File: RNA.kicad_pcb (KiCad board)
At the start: 2 copper layers, 126 x 85 mm, 86 parts, among them J1 USB_B_Micro, J2 AudioJack4, J3 Conn_01x06, SW1 SW_Push, SW11 SW_Push_45deg, SW12 SW_Push_45deg, SW13 SW_Push_45deg, SW14 SW_Push_45deg, SW15 SW_Push_45deg, SW16 SW_Push_45deg, SW2 SW_Push, SW21 SW_Push_45deg, SW22 SW_Push_45deg, SW23 SW_Push_45deg, SW24 SW_Push_45deg, SW25 SW_Push_45deg, SW26 SW_Push_45deg, SW31 SW_Push_45deg, SW32 SW_Push_45deg, SW33 SW_Push_45deg, SW34 SW_Push_45deg, SW35 SW_Push_45deg, SW36 SW_Push_45deg, SW41 SW_Push_45deg, SW42 SW_Push_45deg, SW43 SW_Push_45deg, SW44 SW_Push_45deg, SW45 SW_Push_45deg, SW46 SW_Push_45deg, SW47 SW_Push_45deg, SW51 SW_Push_45deg, SW52 SW_Push_45deg, SW53 SW_Push_45deg, SW54 SW_Push_45deg, SW55 SW_Push_45deg, SW56 SW_Push_45deg, SW57 SW_Push_45deg, U1 STM32F072C8Tx, U2 USBLC6-2SC6, U3 MIC5219-3.3YM5

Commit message: wip"
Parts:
- removed C10, C9: 10u, Capacitor_SMD:C_1206_3216Metric_Pad1.42x1.75mm_HandSolder
- added J4: AudioJack4, Connector_PinHeader_2.54mm:PinHeader_1x04_P2.54mm_Vertical, F.Cu at (133.3, 52.1)
- added R1: R_Small, Resistor_SMD:R_0603_1608Metric, F.Cu at (138.4, 48.0)
- added R2: R_Small, Resistor_SMD:R_0603_1608Metric, F.Cu at (135.9, 48.3)
- added R4: 39k, Resistor_SMD:R_0603_1608Metric, B.Cu at (133.3, 27.9)
- added R7: 68k, Resistor_SMD:R_0603_1608Metric, B.Cu at (133.3, 31.8)
- C1: value 4.7u -> 1u; footprint Capacitor_SMD:C_1206_3216Metric_Pad1.42x1.75mm_HandSolder -> Capacitor_SMD:C_0603_1608Metric
- C2, C3: value 1n -> 100n; footprint Capacitor_SMD:C_0603_1608Metric_Pad1.05x0.95mm_HandSolder -> Capacitor_SMD:C_0603_1608Metric; moved to B.Cu
- C4, J1, U1: moved to B.Cu
- C5: footprint Capacitor_SMD:C_1206_3216Metric_Pad1.42x1.75mm_HandSolder -> Capacitor_SMD:C_0603_1608Metric
- C6, C7: footprint Capacitor_SMD:C_0603_1608Metric_Pad1.05x0.95mm_HandSolder -> Capacitor_SMD:C_0603_1608Metric; moved to B.Cu
- D1: value D_Small -> D_Schottky_Small; footprint Diode_SMD:D_SOD-123 -> Diode_SMD:D_SOD-323
- J2: footprint Connector_Audio:Jack_3.5mm_PJ320E_Horizontal -> Connector_JST:JST_SH_SM04B-SRSS-TB_1x04-1MP_P1.00mm_Horizontal; moved to B.Cu
- J3: footprint Connector_PinSocket_2.54mm:PinSocket_1x06_P2.54mm_Vertical -> Connector_PinHeader_2.54mm:PinHeader_2x03_P2.54mm_Vertical
- R3, R5, R6: footprint Resistor_SMD:R_0603_1608Metric_Pad1.05x0.95mm_HandSolder -> Resistor_SMD:R_0603_1608Metric; moved to B.Cu
- SW1: value SW_Push -> SW_SPST; footprint Button_Switch_SMD:SW_SPST_TL3342 -> Button_Switch_SMD:SW_DIP_SPSTx01_Slide_6.7x4.1mm_W8.61mm_P2.54mm_LowProfile
- SW2: footprint Button_Switch_SMD:SW_SPST_TL3342 -> Button_Switch_SMD:Panasonic_EVQPUL_EVQPUC
- U2: value USBLC6-2SC6 -> PRTR5V0U2X; footprint Package_TO_SOT_SMD:SOT-23-6 -> random-keyboard-parts:SOT143B; moved to B.Cu
- U3: value MIC5219-3.3YM5 -> MCP1703A-3302_SOT23; footprint Package_TO_SOT_SMD:SOT-23-5 -> Package_TO_SOT_SMD:SOT-23
- moved C1 20.6 mm to (131.3, 25.7), turned to 0 degrees
- moved C6 17.2 mm to (130.8, 34.3), turned to 270 degrees
- moved C3 16.9 mm to (138.9, 33.0), turned to 0 degrees
- moved C2 12.9 mm to (143.5, 44.5), turned to 90 degrees
- moved C4 12.6 mm to (132.6, 47.2), turned to 0 degrees
- moved U3 12.4 mm to (133.3, 28.7), turned to 90 degrees
- moved R3 11.5 mm to (141.0, 49.0), turned to 90 degrees
- moved SW2 10.7 mm to (143.5, 67.3)
- moved R5 9.69 mm to (135.9, 61.0)
- moved D1 8.76 mm to (133.3, 32.5), turned to 0 degrees
- moved J3 8.45 mm to (129.5, 63.5)
- moved SW1 8.13 mm to (137.2, 64.8)
- moved J2 7.44 mm to (142.2, 59.7)
- moved R6 7.35 mm to (135.9, 58.4), turned to 180 degrees
- moved U1 6.59 mm to (136.4, 40.2)
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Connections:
- net Net-(U1-Pad39) renamed SWO
- C1 pad 1: VDD -> Net-(C1-Pad1)
- D1 pad 1: Net-(C9-Pad1) -> Net-(C1-Pad1)
- J1 pad 2: Net-(J1-Pad2) -> D-
- J1 pad 3: Net-(J1-Pad3) -> D+
- R5 pad 2: Net-(J2-PadR2) -> Net-(J2-Pad3)
- R6 pad 2: Net-(J2-PadR1) -> Net-(J2-Pad2)
- U1 pad 38: Net-(U1-Pad38) -> VBUS_SENSE
- U1 pad 44: BOOT0 -> Net-(U1-Pad44)
- U1 pad 5: Net-(U1-Pad5) -> BOOT0
- U2 pad 1: Net-(J1-Pad2) -> GND
- U2 pad 2: GND -> D+
- U2 pad 3: Net-(J1-Pad3) -> D-
- U2 pad 4: D+ -> VBUS
- U3 pad 1: Net-(C9-Pad1) -> GND
- U3 pad 2: GND -> VDD
- U3 pad 3: Net-(C9-Pad1) -> Net-(C1-Pad1)
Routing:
- net VBUS_SENSE: track 0.00 -> 2.23 mm
- net (no net): vias 2 -> 0

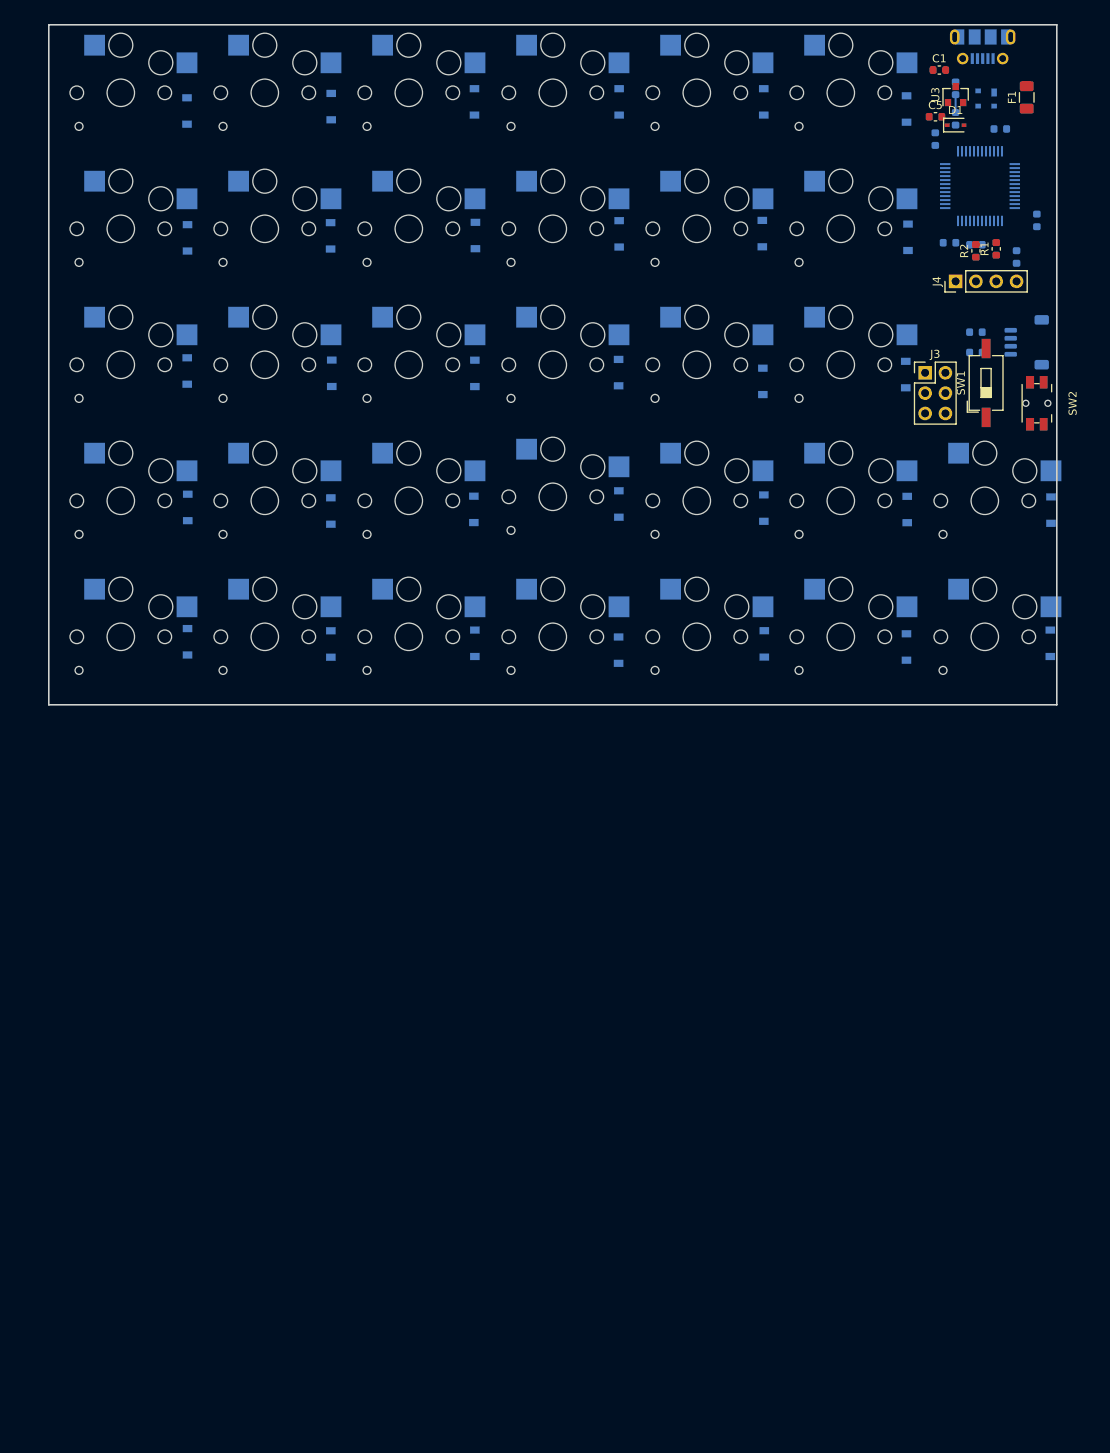
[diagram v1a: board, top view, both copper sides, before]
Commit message: fix pcb size
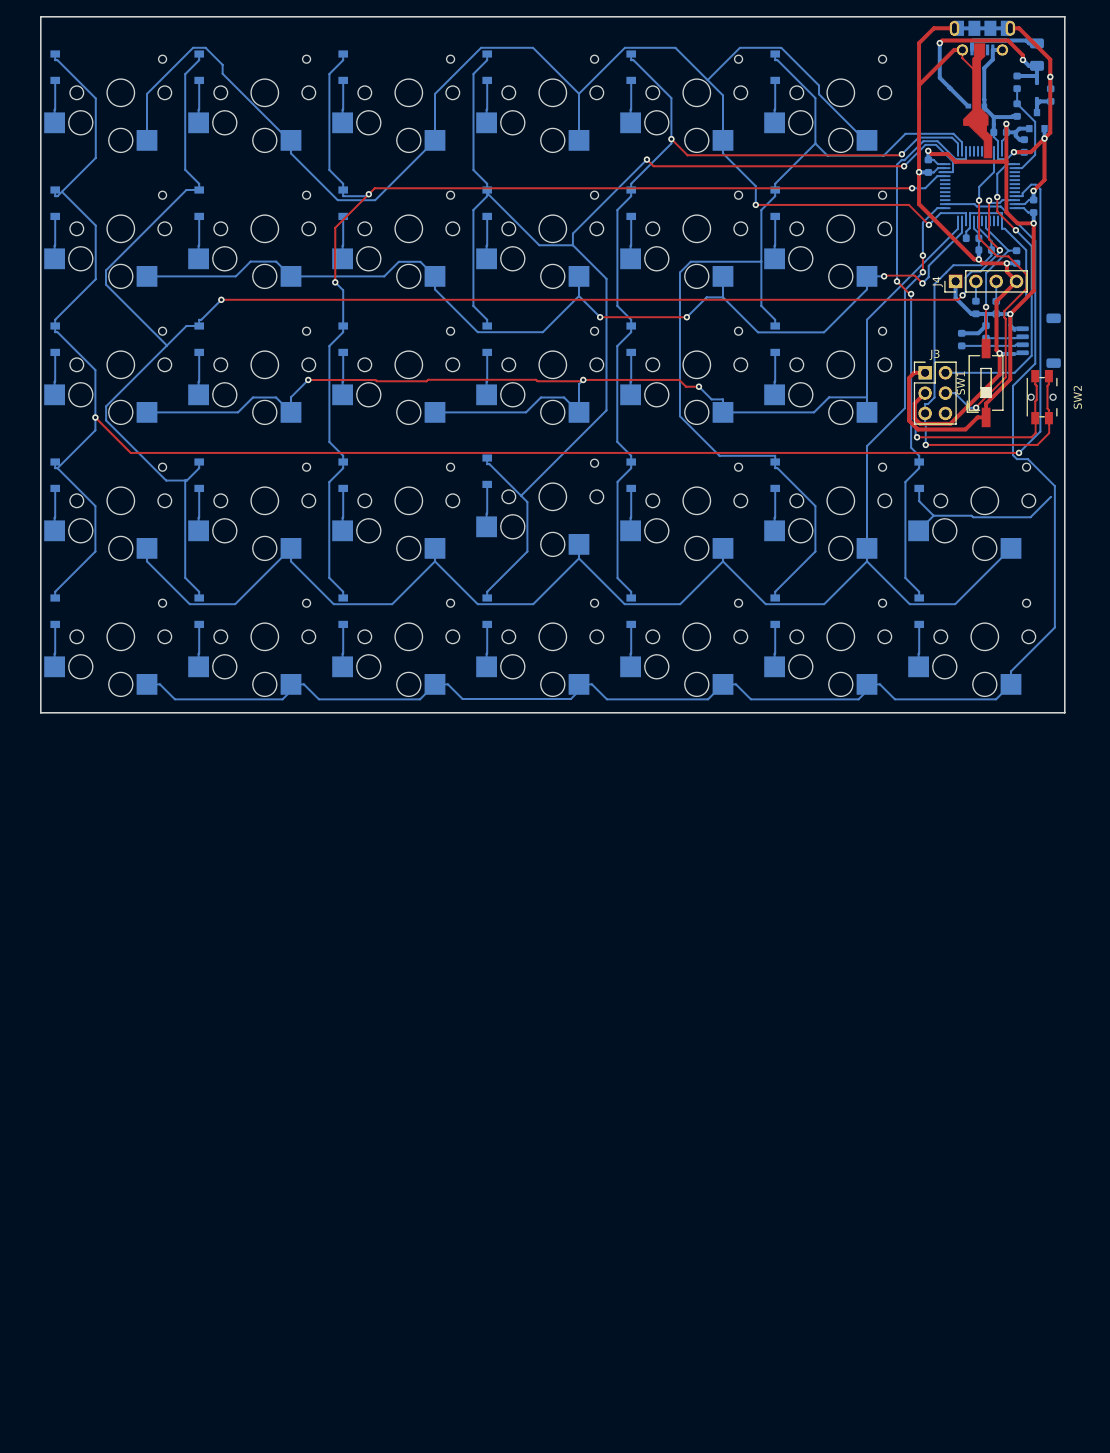
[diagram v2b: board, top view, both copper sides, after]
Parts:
- C1, C5, D1, F1, R1, R2, U3: moved to B.Cu
- C4, C6: value 1n -> 100n
- moved D11 17.4 mm to (20.8, 25.3), turned to 270 degrees
- moved D35 17.3 mm to (92.8, 59.3), turned to 270 degrees
- moved D16 17.2 mm to (110.8, 25.3), turned to 270 degrees
- moved D12 17.2 mm to (38.8, 25.3), turned to 270 degrees
- moved D26 17.1 mm to (110.8, 42.3), turned to 270 degrees
- moved D54 17.1 mm to (74.8, 93.3), turned to 270 degrees
- moved D55 17.1 mm to (92.8, 93.3), turned to 270 degrees
- moved D15 17.1 mm to (92.8, 25.3), turned to 270 degrees
- moved D32 17.1 mm to (38.8, 59.3), turned to 270 degrees
- moved D21 17.1 mm to (20.8, 42.3), turned to 270 degrees
- moved D45 17.1 mm to (92.8, 76.3), turned to 270 degrees
- moved D42 17.1 mm to (38.8, 76.3), turned to 270 degrees
- moved D41 17.1 mm to (20.8, 76.3), turned to 270 degrees
- moved D14 17.1 mm to (74.8, 25.3), turned to 270 degrees
- moved D46 17.0 mm to (110.8, 76.3), turned to 270 degrees
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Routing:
- net COL1: track 0.00 -> 242.6 mm, vias 0 -> 2
- net COL2: track 0.00 -> 211.9 mm, vias 0 -> 4
- net ROW5: track 0.00 -> 194.7 mm
- net ROW4: track 0.00 -> 193.3 mm, vias 0 -> 2
- net GND: track 0.00 -> 189.4 mm, vias 0 -> 9
- net ROW1: track 0.00 -> 185.4 mm, vias 0 -> 2
- net COL4: track 0.00 -> 167.7 mm, vias 0 -> 2
- net COL3: track 0.00 -> 151.0 mm, vias 0 -> 3
- net ROW3: track 0.00 -> 150.5 mm, vias 0 -> 3
- net ROW2: track 0.00 -> 128.9 mm, vias 0 -> 4
- net VDD: track 0.00 -> 127.8 mm, vias 0 -> 4
- net COL6: track 0.00 -> 126.2 mm
- net COL5: track 0.00 -> 115.5 mm, vias 0 -> 2
- net COL7: track 0.00 -> 68.6 mm, vias 0 -> 2
- net NRST: track 0.00 -> 57.8 mm, vias 0 -> 1
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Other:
- board size 126 x 85 mm -> 128 x 87 mm

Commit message: add sub(right-hand) keyboard
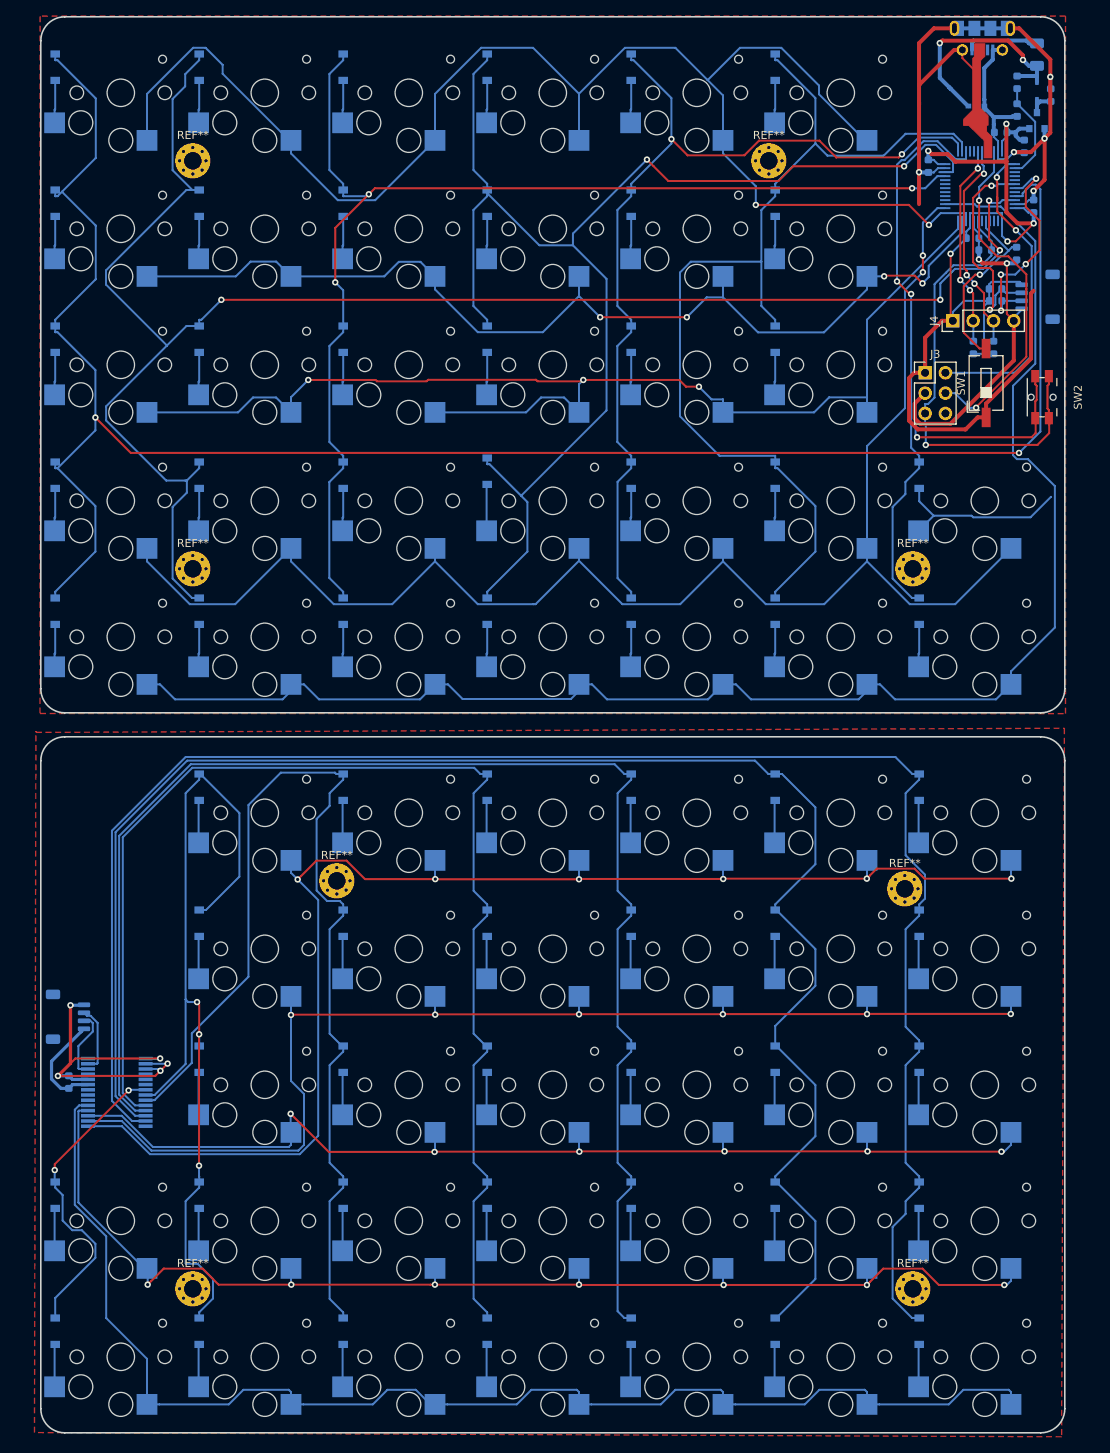
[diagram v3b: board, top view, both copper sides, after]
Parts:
- added C8: C_Small, Capacitor_SMD:C_0603_1608Metric, B.Cu at (22.5, 152.2)
- added D12S1: D_Small, Diode_SMD:D_SOD-123, B.Cu at (38.8, 115.3)
- added D13S1: D_Small, Diode_SMD:D_SOD-123, B.Cu at (56.8, 115.3)
- added D14S1: D_Small, Diode_SMD:D_SOD-123, B.Cu at (74.8, 115.3)
- added D15S1: D_Small, Diode_SMD:D_SOD-123, B.Cu at (92.8, 115.3)
- added D16S1: D_Small, Diode_SMD:D_SOD-123, B.Cu at (110.8, 115.3)
- added D17S1: D_Small, Diode_SMD:D_SOD-123, B.Cu at (128.8, 115.3)
- added D22S1: D_Small, Diode_SMD:D_SOD-123, B.Cu at (38.8, 132.3)
- added D23S1: D_Small, Diode_SMD:D_SOD-123, B.Cu at (56.8, 132.3)
- added D24S1: D_Small, Diode_SMD:D_SOD-123, B.Cu at (74.8, 132.3)
- added D25S1: D_Small, Diode_SMD:D_SOD-123, B.Cu at (92.8, 132.3)
- added D26S1: D_Small, Diode_SMD:D_SOD-123, B.Cu at (110.8, 132.3)
- added D27S1: D_Small, Diode_SMD:D_SOD-123, B.Cu at (128.8, 132.3)
- added D32S1: D_Small, Diode_SMD:D_SOD-123, B.Cu at (38.8, 149.3)
- added D33S1: D_Small, Diode_SMD:D_SOD-123, B.Cu at (56.8, 149.3)
- added D34S1: D_Small, Diode_SMD:D_SOD-123, B.Cu at (74.8, 149.3)
- added D35S1: D_Small, Diode_SMD:D_SOD-123, B.Cu at (92.8, 149.3)
- added D36S1: D_Small, Diode_SMD:D_SOD-123, B.Cu at (110.8, 149.3)
- added D37S1: D_Small, Diode_SMD:D_SOD-123, B.Cu at (128.8, 149.3)
- added D41S1: D_Small, Diode_SMD:D_SOD-123, B.Cu at (20.8, 166.3)
- added D42S1: D_Small, Diode_SMD:D_SOD-123, B.Cu at (38.8, 166.3)
- added D43S1: D_Small, Diode_SMD:D_SOD-123, B.Cu at (56.8, 166.3)
- added D44S1: D_Small, Diode_SMD:D_SOD-123, B.Cu at (74.8, 166.3)
- added D45S1: D_Small, Diode_SMD:D_SOD-123, B.Cu at (92.8, 166.3)
- added D46S1: D_Small, Diode_SMD:D_SOD-123, B.Cu at (110.8, 166.3)
- added D47S1: D_Small, Diode_SMD:D_SOD-123, B.Cu at (128.8, 166.3)
- added D51S1: D_Small, Diode_SMD:D_SOD-123, B.Cu at (20.8, 183.3)
- added D52S1: D_Small, Diode_SMD:D_SOD-123, B.Cu at (38.8, 183.3)
- added D53S1: D_Small, Diode_SMD:D_SOD-123, B.Cu at (56.8, 183.3)
- added D54S1: D_Small, Diode_SMD:D_SOD-123, B.Cu at (74.8, 183.3)
- added D55S1: D_Small, Diode_SMD:D_SOD-123, B.Cu at (92.8, 183.3)
- added D56S1: D_Small, Diode_SMD:D_SOD-123, B.Cu at (110.8, 183.3)
- added D57S1: D_Small, Diode_SMD:D_SOD-123, B.Cu at (128.8, 183.3)
- added J5: AudioJack4, Connector_JST:JST_SH_SM04B-SRSS-TB_1x04-1MP_P1.00mm_Horizontal, B.Cu at (22.4, 144.0)
- added REF**: MountingHole_2.2mm_M2_Pad_Via, MountingHole:MountingHole_2.2mm_M2_Pad_Via, F.Cu at (127.0, 128.0)
- added REF**: MountingHole_2.2mm_M2_Pad_Via, MountingHole:MountingHole_2.2mm_M2_Pad_Via, F.Cu at (128.0, 178.0)
- added REF**: MountingHole_2.2mm_M2_Pad_Via, MountingHole:MountingHole_2.2mm_M2_Pad_Via, F.Cu at (38.0, 178.0)
- added REF**: MountingHole_2.2mm_M2_Pad_Via, MountingHole:MountingHole_2.2mm_M2_Pad_Via, F.Cu at (56.0, 127.0)
- added REF**: MountingHole_2.2mm_M2_Pad_Via, MountingHole:MountingHole_2.2mm_M2_Pad_Via, F.Cu at (38.0, 37.0)
- added REF**: MountingHole_2.2mm_M2_Pad_Via, MountingHole:MountingHole_2.2mm_M2_Pad_Via, F.Cu at (38.0, 88.0)
- added REF**: MountingHole_2.2mm_M2_Pad_Via, MountingHole:MountingHole_2.2mm_M2_Pad_Via, F.Cu at (128.0, 88.0)
- added REF**: MountingHole_2.2mm_M2_Pad_Via, MountingHole:MountingHole_2.2mm_M2_Pad_Via, F.Cu at (110.0, 37.0)
- added SW12S1: SW_Push_45deg, keyswitches:PG1350_socket, F.Cu at (47.0, 118.5)
- added SW13S1: SW_Push_45deg, keyswitches:PG1350_socket, F.Cu at (65.0, 118.5)
- added SW14S1: SW_Push_45deg, keyswitches:PG1350_socket, F.Cu at (83.0, 118.5)
- added SW15S1: SW_Push_45deg, keyswitches:PG1350_socket, F.Cu at (101.0, 118.5)
- added SW16S1: SW_Push_45deg, keyswitches:PG1350_socket, F.Cu at (119.0, 118.5)
- added SW17S1: SW_Push_45deg, keyswitches:PG1350_socket, F.Cu at (137.0, 118.5)
- added SW22S1: SW_Push_45deg, keyswitches:PG1350_socket, F.Cu at (47.0, 135.5)
- added SW23S1: SW_Push_45deg, keyswitches:PG1350_socket, F.Cu at (65.0, 135.5)
- added SW24S1: SW_Push_45deg, keyswitches:PG1350_socket, F.Cu at (83.0, 135.5)
- added SW25S1: SW_Push_45deg, keyswitches:PG1350_socket, F.Cu at (101.0, 135.5)
- added SW26S1: SW_Push_45deg, keyswitches:PG1350_socket, F.Cu at (119.0, 135.5)
- added SW27S1: SW_Push_45deg, keyswitches:PG1350_socket, F.Cu at (137.0, 135.5)
- added SW32S1: SW_Push_45deg, keyswitches:PG1350_socket, F.Cu at (47.0, 152.5)
- added SW33S1: SW_Push_45deg, keyswitches:PG1350_socket, F.Cu at (65.0, 152.5)
- added SW34S1: SW_Push_45deg, keyswitches:PG1350_socket, F.Cu at (83.0, 152.5)
- added SW35S1: SW_Push_45deg, keyswitches:PG1350_socket, F.Cu at (101.0, 152.5)
- added SW36S1: SW_Push_45deg, keyswitches:PG1350_socket, F.Cu at (119.0, 152.5)
- added SW37S1: SW_Push_45deg, keyswitches:PG1350_socket, F.Cu at (137.0, 152.5)
- added SW41S1: SW_Push_45deg, keyswitches:PG1350_socket, F.Cu at (29.0, 169.5)
- added SW42S1: SW_Push_45deg, keyswitches:PG1350_socket, F.Cu at (47.0, 169.5)
- added SW43S1: SW_Push_45deg, keyswitches:PG1350_socket, F.Cu at (65.0, 169.5)
- added SW44S1: SW_Push_45deg, keyswitches:PG1350_socket, F.Cu at (83.0, 169.5)
- added SW45S1: SW_Push_45deg, keyswitches:PG1350_socket, F.Cu at (101.0, 169.5)
- added SW46S1: SW_Push_45deg, keyswitches:PG1350_socket, F.Cu at (119.0, 169.5)
- added SW47S1: SW_Push_45deg, keyswitches:PG1350_socket, F.Cu at (137.0, 169.5)
- added SW51S1: SW_Push_45deg, keyswitches:PG1350_socket, F.Cu at (29.0, 186.5)
- added SW52S1: SW_Push_45deg, keyswitches:PG1350_socket, F.Cu at (47.0, 186.5)
- added SW53S1: SW_Push_45deg, keyswitches:PG1350_socket, F.Cu at (65.0, 186.5)
- added SW54S1: SW_Push_45deg, keyswitches:PG1350_socket, F.Cu at (83.0, 186.5)
- added SW55S1: SW_Push_45deg, keyswitches:PG1350_socket, F.Cu at (101.0, 186.5)
- added SW56S1: SW_Push_45deg, keyswitches:PG1350_socket, F.Cu at (119.0, 186.5)
- added SW57S1: SW_Push_45deg, keyswitches:PG1350_socket, F.Cu at (137.0, 186.5)
- added U4: MCP23017_SS, Package_SO:SSOP-28_5.3x10.2mm_P0.65mm, B.Cu at (28.5, 153.4)
- moved R5 6.43 mm to (138.3, 54.5), turned to 0 degrees
- moved R6 5.51 mm to (138.3, 53.0), turned to 0 degrees
- moved J2 5.49 mm to (143.6, 54.0)
- moved R2 5.01 mm to (135.6, 60.3)
- moved R1 4.99 mm to (138.1, 60.3)
- moved J4 4.94 mm to (133.0, 57.0)
- moved SW44 0.50 mm to (83.0, 79.5)
- moved R3 0.43 mm to (141.0, 48.6)
- moved C3 0.08 mm to (139.0, 33.5)
- moved C5 0.05 mm to (141.9, 35.2)
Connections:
- J2 pad 2: Net-(J2-Pad2) -> SCL1
- J2 pad 3: Net-(J2-Pad3) -> SDA1
- J4 pad 2: Net-(J4-Pad2) -> SCL2
- J4 pad 3: Net-(J4-Pad3) -> SDA2
- R1 pad 2: Net-(J4-Pad3) -> SDA2
- R2 pad 2: Net-(J4-Pad2) -> SCL2
- R5 pad 2: Net-(J2-Pad3) -> SDA1
- R6 pad 2: Net-(J2-Pad2) -> SCL1
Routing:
- net COL7S: track 0.00 -> 221.0 mm
- net COL6S: track 0.00 -> 210.1 mm
- net COL5S: track 0.00 -> 178.8 mm
- net ROW1S: track 0.00 -> 170.9 mm, vias 0 -> 6
- net ROW5S: track 0.00 -> 164.1 mm
- net COL4S: track 0.00 -> 158.7 mm
- net ROW4S: track 0.00 -> 150.0 mm, vias 0 -> 7
- net ROW2S: track 0.00 -> 149.3 mm, vias 0 -> 6
- net ROW3S: track 0.00 -> 134.7 mm, vias 0 -> 6
- net COL3S: track 0.00 -> 132.6 mm
- net COL2S: track 0.00 -> 111.6 mm, vias 0 -> 3
- net COL1S: track 0.00 -> 39.3 mm, vias 0 -> 2
- net GND: track 189.4 -> 227.1 mm, vias 9 -> 13
- net SCL1: track 0.00 -> 28.0 mm, vias 0 -> 2
- net SDA1: track 0.00 -> 27.8 mm, vias 0 -> 4
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- added copper zone on F.Cu, net GND
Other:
- board size 128 x 87 mm -> 128 x 177 mm

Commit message: ready to alpha
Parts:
- removed R4: 39k, Resistor_SMD:R_0603_1608Metric
- removed R7: 68k, Resistor_SMD:R_0603_1608Metric
- added C9: C_Small, Capacitor_SMD:C_0603_1608Metric, B.Cu at (134.2, 69.6)
- added U5: CAT24M01W, Package_SO:SOIC-8_3.9x4.9mm_P1.27mm, B.Cu at (135.8, 74.0)
- C7: value C_Small -> 100u
- moved REF** 1.41 mm to (128.0, 127.0)
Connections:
- J3 pad 6: Net-(J3-Pad6) -> SWO
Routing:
- net SWO: track 0.00 -> 62.4 mm, vias 0 -> 4
- net SCL1: track 28.0 -> 72.9 mm, vias 2 -> 5
- net SDA1: track 27.8 -> 51.4 mm, vias 4 -> 6
- net VBUS_SENSE: track 12.4 -> 0.00 mm
- net VDD: track 149.5 -> 159.6 mm, vias 5 -> 6
- net GND: track 227.1 -> 236.1 mm, vias 13 -> 16
- net ROW1S: track 170.9 -> 174.3 mm
- net VBUS: track 28.2 -> 25.7 mm
- net COL7S: track 221.0 -> 222.7 mm
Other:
- board size 128 x 177 mm -> 134 x 177 mm

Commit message: update annotation
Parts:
- renumbered C2 to C1, C3 to C2, C4 to C3, C6 to C4, C7 to C5, C1 to C6, C5 to C7, C9 to C8, C8 to C9, D42 to D10, D52 to D11, D13 to D12, D23 to D13, D33 to D14, D43 to D15, D53 to D16, D14 to D17, D24 to D18, D34 to D19, D11 to D2, D44 to D20, D54 to D21, D15 to D22, D25 to D23, D35 to D24, D45 to D25, D55 to D26, D16 to D27, D26 to D28, D36 to D29, D21 to D3, D46 to D30, D56 to D31, D47 to D32, D57 to D33, D41S1 to D34, D51S1 to D35, D12S1 to D36, D22S1 to D37, D32S1 to D38, D42S1 to D39, D31 to D4, D52S1 to D40, D13S1 to D41, D23S1 to D42, D33S1 to D43, D43S1 to D44, D53S1 to D45, D14S1 to D46, D24S1 to D47, D34S1 to D48, D44S1 to D49, D41 to D5, D54S1 to D50, D15S1 to D51, D25S1 to D52, D35S1 to D53, D45S1 to D54, D55S1 to D55, D16S1 to D56, D26S1 to D57, D36S1 to D58, D46S1 to D59, D51 to D6, D56S1 to D60, D17S1 to D61, D27S1 to D62, D37S1 to D63, D47S1 to D64, D57S1 to D65, D12 to D7, D22 to D8, D32 to D9, J4 to J2, J2 to J3, J3 to J4, R3 to R1, R1 to R2, R2 to R3, R5 to R4, R6 to R5, SW32 to SW10, SW42 to SW11, SW52 to SW12, SW23 to SW14, SW33 to SW15, SW43 to SW16, SW53 to SW17, SW14 to SW18, SW24 to SW19, SW34 to SW20, SW44 to SW21, SW54 to SW22, SW15 to SW23, SW25 to SW24, SW35 to SW25, SW45 to SW26, SW55 to SW27, SW16 to SW28, SW26 to SW29, SW11 to SW3, SW36 to SW30, SW46 to SW31, SW56 to SW32, SW47 to SW33, SW57 to SW34, SW41S1 to SW35, SW51S1 to SW36, SW12S1 to SW37, SW22S1 to SW38, SW32S1 to SW39, SW21 to SW4, SW42S1 to SW40, SW52S1 to SW41, SW13S1 to SW42, SW23S1 to SW43, SW33S1 to SW44, SW43S1 to SW45, SW53S1 to SW46, SW14S1 to SW47, SW24S1 to SW48, SW34S1 to SW49, SW31 to SW5, SW44S1 to SW50, SW54S1 to SW51, SW15S1 to SW52, SW25S1 to SW53, SW35S1 to SW54, SW45S1 to SW55, SW55S1 to SW56, SW16S1 to SW57, SW26S1 to SW58, SW36S1 to SW59, SW41 to SW6, SW46S1 to SW60, SW56S1 to SW61, SW17S1 to SW62, SW27S1 to SW63, SW37S1 to SW64, SW47S1 to SW65, SW57S1 to SW66, SW51 to SW7, SW12 to SW8, SW22 to SW9, U5 to U4, U4 to U5

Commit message: modify module
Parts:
- C8, C9: value C_Small -> 100n
- D1: value D_Schottky_Small -> B5817WS
- D10, D11, D12, D13, D14, D15, D16, D17, D18, D19, D2, D20, D21, D22, D23, D24, D25, D26, D27, D28, D29, D3, D30, D31, D32, D33, D34, D35, D36, D37, D38, D39, D4, D40, D41, D42, D43, D44, D45, D46, D47, D48, D49, D5, D50, D51, D52, D53, D54, D55, D56, D57, D58, D59, D6, D60, D61, D62, D63, D64, D65, D7, D8, D9: value D_Small -> 1N4148W
- R2, R3, R4, R5: value R_Small -> 2.2k
- SW10, SW11, SW12, SW13, SW14, SW15, SW16, SW17, SW18, SW19, SW20, SW21, SW22, SW23, SW24, SW25, SW26, SW27, SW28, SW29, SW3, SW30, SW31, SW32, SW33, SW34, SW35, SW36, SW37, SW38, SW39, SW4, SW40, SW41, SW42, SW43, SW44, SW45, SW46, SW47, SW48, SW49, SW5, SW50, SW51, SW52, SW53, SW54, SW55, SW56, SW57, SW58, SW59, SW6, SW60, SW61, SW62, SW63, SW64, SW65, SW66, SW7, SW8, SW9: value SW_Push_45deg -> CPG135001S30
